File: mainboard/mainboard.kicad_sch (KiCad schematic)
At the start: 52 parts, among them J1 Servo, J2 Buzzer, J4 Button Interface, J5 Power, J6 Release Button, J7 Extra Pins, Q1 BSS138, SW1 SW_Push, U1 RP2040, U2 W25Q128JVS, U3 RV-3028-C7, U4 ITR9608-F, Y1 Crystal_ABM8

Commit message: updated battery footprint
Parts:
- BT1: footprint Battery:BatteryHolder_MPD_BC2003_1x2032 -> Battery:BatteryHolder_Keystone_1060_1x2032
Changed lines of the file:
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@@
 			)
 		)
-		(property "Footprint" "Battery:BatteryHolder_MPD_BC2003_1x2032"
+		(property "Footprint" "Battery:BatteryHolder_Keystone_1060_1x2032"
 			(at 267.97 147.066 90)
 			(effects

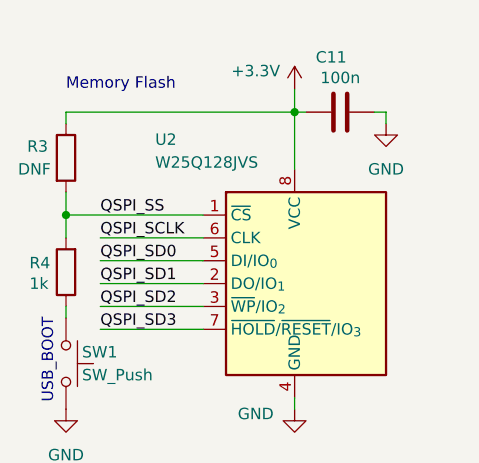
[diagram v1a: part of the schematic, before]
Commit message: switched resistors and capacitors to 0402 and updated pcb
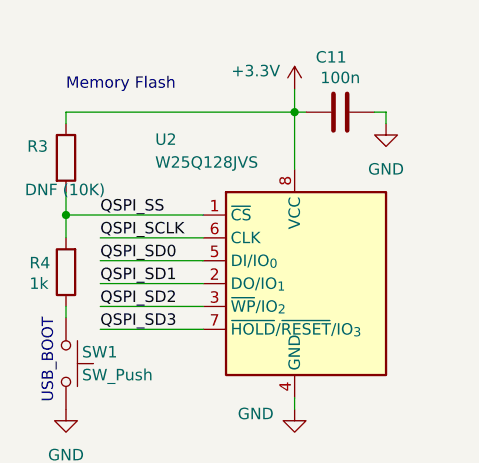
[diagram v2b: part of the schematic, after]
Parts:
- D1, D2: footprint LED_SMD:LED_1206_3216Metric -> LED_SMD:LED_0402_1005Metric
- R10, R11, R12, R13, R22, R6, R7, R8, R9: footprint Resistor_SMD:R_0805_2012Metric -> Resistor_SMD:R_0402_1005Metric
- R14, R4: footprint Resistor_SMD:R_0603_1608Metric -> Resistor_SMD:R_0402_1005Metric
- R3: value DNF -> DNF (10K)
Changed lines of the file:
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@@
 			)
 		)
-		(property "Footprint" "Resistor_SMD:R_0805_2012Metric"
+		(property "Footprint" "Resistor_SMD:R_0402_1005Metric"
 			(at 224.282 100.33 90)
 			(effects
@@
 			)
 		)
-		(property "Footprint" "LED_SMD:LED_1206_3216Metric"
+		(property "Footprint" "LED_SMD:LED_0402_1005Metric"
 			(at 232.41 35.56 0)
 			(effects
@@
 			)
 		)
-		(property "Footprint" "Resistor_SMD:R_0805_2012Metric"
+		(property "Footprint" "Resistor_SMD:R_0402_1005Metric"
 			(at 220.472 135.89 90)
 			(effects
@@
 			)
 		)
-		(property "Footprint" "Resistor_SMD:R_0603_1608Metric"
+		(property "Footprint" "Resistor_SMD:R_0402_1005Metric"
 			(at 23.368 41.91 90)
 			(effects
@@
 			)
 		)
-		(property "Footprint" "Resistor_SMD:R_0805_2012Metric"
+		(property "Footprint" "Resistor_SMD:R_0402_1005Metric"
 			(at 257.302 134.62 90)
 			(effects
@@
 			)
 		)
-		(property "Footprint" "Resistor_SMD:R_0603_1608Metric"
+		(property "Footprint" "Resistor_SMD:R_0402_1005Metric"
 			(at 195.58 41.148 90)
 			(effects
@@
 			)
 		)
-		(property "Footprint" "LED_SMD:LED_1206_3216Metric"
+		(property "Footprint" "LED_SMD:LED_0402_1005Metric"
 			(at 219.71 35.56 0)
 			(effects
@@
 			)
 		)
-		(property "Footprint" "Resistor_SMD:R_0805_2012Metric"
+		(property "Footprint" "Resistor_SMD:R_0402_1005Metric"
 			(at 243.332 100.33 90)
 			(effects
@@
 			)
 		)
-		(property "Footprint" "Resistor_SMD:R_0805_2012Metric"
+		(property "Footprint" "Resistor_SMD:R_0402_1005Metric"
 			(at 60.452 82.55 90)
 			(effects
@@
 			)
 		)
-		(property "Footprint" "Resistor_SMD:R_0805_2012Metric"
+		(property "Footprint" "Resistor_SMD:R_0402_1005Metric"
 			(at 210.312 135.89 90)
 			(effects
@@
 			)
 		)
-		(property "Footprint" "Resistor_SMD:R_0805_2012Metric"
+		(property "Footprint" "Resistor_SMD:R_0402_1005Metric"
 			(at 230.632 27.94 90)
 			(effects
@@
 			)
 		)
-		(property "Footprint" "Resistor_SMD:R_0805_2012Metric"
+		(property "Footprint" "Resistor_SMD:R_0402_1005Metric"
 			(at 160.782 105.41 90)
 			(effects
@@
 			)
 		)
-		(property "Footprint" "Resistor_SMD:R_0805_2012Metric"
+		(property "Footprint" "Resistor_SMD:R_0402_1005Metric"
 			(at 217.932 27.94 90)
 			(effects
@@
 			)
 		)
-		(property "Value" "DNF"
-			(at 16.256 30.48 0)
+		(property "Value" "DNF (10K)"
+			(at 17.018 32.766 0)
 			(effects
 				(font

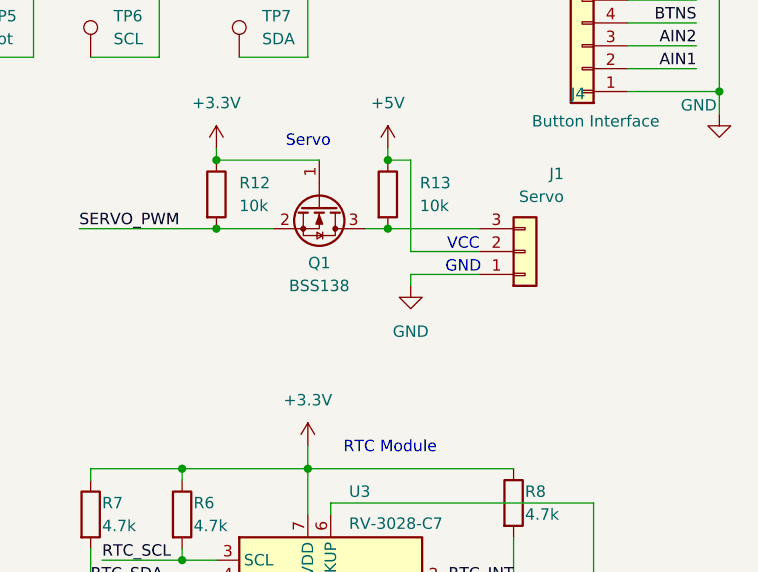
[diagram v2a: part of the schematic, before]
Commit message: added indicator LEDs
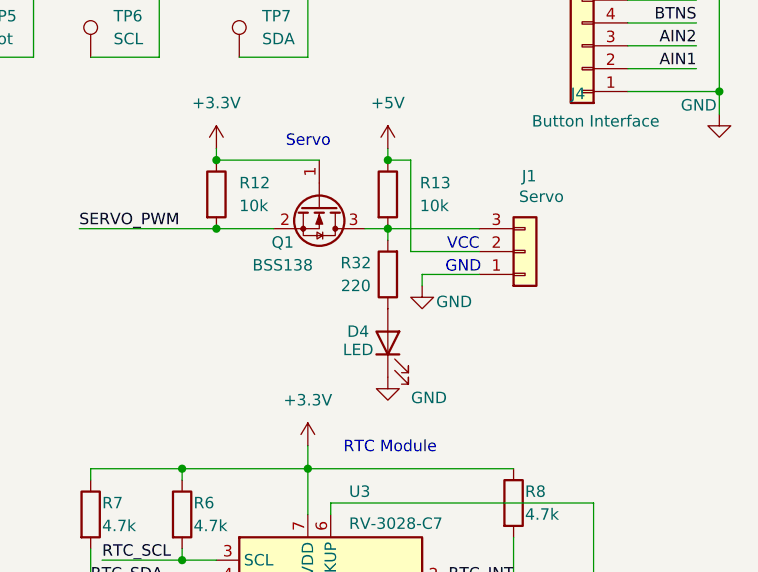
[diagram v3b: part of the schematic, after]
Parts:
- added D4: LED, LED_SMD:LED_0402_1005Metric, symbol Device:LED
- added R32: 220, Resistor_SMD:R_0402_1005Metric, symbol Device:R
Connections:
- net GND: now also D4.1 (K)
- net at J1.3 (Pin_3), Q1.3 (D), R13.2: now also R32.2
- new net: D4.2 (A), R32.1
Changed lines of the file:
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@@
 	(wire
 		(pts
-			(xy 247.65 109.22) (xy 247.65 110.49)
+			(xy 248.92 109.22) (xy 248.92 110.49)
 		)
 		(stroke
@@
 	(wire
 		(pts
-			(xy 247.65 109.22) (xy 255.27 109.22)
+			(xy 248.92 109.22) (xy 255.27 109.22)
 		)
 		(stroke
@@
 	(wire
 		(pts
+			(xy 245.11 104.14) (xy 245.11 105.41)
+		)
+		(stroke
+			(width 0)
+			(type default)
+		)
+	)
+	(wire
+		(pts
 			(xy 71.12 72.39) (xy 71.12 76.2)
 		)
@@
 		(dnp no)
 		(property "Reference" "J1"
-			(at 264.668 98.044 0)
+			(at 261.62 98.298 0)
 			(effects
 				(font
@@
 	)
 	(symbol
+		(lib_id "Device:LED")
+		(at 245.11 116.84 90)
+		(unit 1)
+		(exclude_from_sim no)
+		(in_bom yes)
+		(on_board yes)
+		(dnp no)
+		(property "Reference" "D4"
+			(at 241.808 115.57 90)
+			(effects
+				(font
+					(size 1.27 1.27)
+				)
+			)
+		)
+		(property "Value" "LED"
+			(at 241.808 117.602 90)
+			(effects
+				(font
+					(size 1.27 1.27)
+				)
+			)
+		)
+		(property "Footprint" "LED_SMD:LED_0402_1005Metric"
+			(at 245.11 116.84 0)
+			(effects
+				(font
+					(size 1.27 1.27)
+				)
+				(hide yes)
+			)
+		)
+		(property "Datasheet" "~"
+			(at 245.11 116.84 0)
+			(effects
+				(font
+					(size 1.27 1.27)
+				)
+				(hide yes)
+			)
+		)
+		(property "Description" "White LED"
+			(at 245.11 116.84 0)
+			(effects
+				(font
+					(size 1.27 1.27)
+				)
+				(hide yes)
+			)
+		)
+		(property "Sim.Pins" "1=K 2=A"
+			(at 245.11 116.84 0)
+			(effects
+				(font
+					(size 1.27 1.27)
+				)
+				(hide yes)
+			)
+		)
+		(pin "2"
+		)
+		(pin "1"
+		)
+		(instances
+			(project "mainboard"
+				(path "/57f2b6ac-3611-4b16-b8a1-8e91b00e0208"
+					(reference "D4")
+					(unit 1)
+				)
+			)
+		)
+	)
+	(symbol
 		(lib_id "Device:R")
 		(at 21.59 41.91 180)
@@
 		(on_board yes)
 		(dnp no)
-		(fields_autoplaced yes)
 		(property "Reference" "Q1"
-			(at 237.49 107.95 90)
+			(at 233.426 105.664 90)
 			(effects
 				(font
@@
 		)
 		(property "Value" "BSS138"
-			(at 237.49 110.49 90)
+			(at 233.426 108.204 90)
 			(effects
 				(font
@@
 	)
 	(symbol
+		(lib_id "power:GND")
+		(at 245.11 120.65 0)
+		(unit 1)
+		(exclude_from_sim no)
+		(in_bom yes)
+		(on_board yes)
+		(dnp no)
+		(property "Reference" "#PWR035"
+			(at 245.11 127 0)
+			(effects
+				(font
+					(size 1.27 1.27)
+				)
+				(hide yes)
+			)
+		)
+		(property "Value" "GND"
+			(at 249.682 122.936 0)
+			(effects
+				(font
+					(size 1.27 1.27)
+				)
+			)
+		)
+		(property "Footprint" ""
+			(at 245.11 120.65 0)
+			(effects
+				(font
+					(size 1.27 1.27)
+				)
+				(hide yes)
+			)
+		)
+		(property "Datasheet" ""
+			(at 245.11 120.65 0)
+			(effects
+				(font
+					(size 1.27 1.27)
+				)
+				(hide yes)
+			)
+		)
+		(property "Description" "Power symbol creates a global label with name \"GND\" , ground"
+			(at 245.11 120.65 0)
+			(effects
+				(font
+					(size 1.27 1.27)
+				)
+				(hide yes)
+			)
+		)
+		(pin "1"
+		)
+		(instances
+			(project ""
+				(path "/57f2b6ac-3611-4b16-b8a1-8e91b00e0208"
+					(reference "#PWR035")
+					(unit 1)
+				)
+			)
+		)
+	)
+	(symbol
 		(lib_id "Device:C")
 		(at 109.22 53.34 180)
@@
 	(symbol
 		(lib_id "power:GND")
-		(at 247.65 110.49 0)
+		(at 248.92 110.49 0)
 		(unit 1)
 		(exclude_from_sim no)
@@
 		(on_board yes)
 		(dnp no)
-		(fields_autoplaced yes)
 		(property "Reference" "#PWR013"
-			(at 247.65 116.84 0)
+			(at 248.92 116.84 0)
 			(effects
 				(font
@@
 		)
 		(property "Value" "GND"
-			(at 247.65 115.57 0)
+			(at 252.476 112.268 0)
 			(effects
 				(font
@@
 		)
 		(property "Footprint" ""
-			(at 247.65 110.49 0)
+			(at 248.92 110.49 0)
 			(effects
 				(font
@@
 		)
 		(property "Datasheet" ""
-			(at 247.65 110.49 0)
+			(at 248.92 110.49 0)
 			(effects
 				(font
@@
 		)
 		(property "Description" "Power symbol creates a global label with name \"GND\" , ground"
-			(at 247.65 110.49 0)
+			(at 248.92 110.49 0)
 			(effects
 				(font
@@
 					(unit 1)
 				)
+			)
+		)
+	)
+	(symbol
+		(lib_id "Device:R")
+		(at 245.11 109.22 180)
+		(unit 1)
+		(exclude_from_sim no)
+		(in_bom yes)
+		(on_board yes)
+		(dnp no)
+		(property "Reference" "R32"
+			(at 241.554 107.95 0)
+			(effects
+				(font
+					(size 1.27 1.27)
+				)
+			)
+		)
+		(property "Value" "220"
+			(at 241.554 110.49 0)
+			(effects
+				(font
+					(size 1.27 1.27)
+				)
+			)
+		)
+		(property "Footprint" "Resistor_SMD:R_0402_1005Metric"
+			(at 246.888 109.22 90)
+			(effects
+				(font
+					(size 1.27 1.27)
+				)
+				(hide yes)
+			)
+		)
+		(property "Datasheet" "~"
+			(at 245.11 109.22 0)
+			(effects
+				(font
+					(size 1.27 1.27)
+				)
+				(hide yes)
+			)
+		)
+		(property "Description" "Resistor"
+			(at 245.11 109.22 0)
+			(effects
+				(font
+					(size 1.27 1.27)
+				)
+				(hide yes)
+			)
+		)
+		(pin "2"
+		)
+		(pin "1"
+		)
+		(instances
+			(project "mainboard"
+				(path "/57f2b6ac-3611-4b16-b8a1-8e91b00e0208"
+					(reference "R32")
+					(unit 1)
+				)

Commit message: Minor fixes
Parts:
- removed R12: 10k, Resistor_SMD:R_0402_1005Metric, symbol Device:R
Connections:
- net +3.3V: no longer Q1.1 (G)
- net GND: now also Q1.2 (S)
- net SERVO_PWM: now also Q1.1 (G), R32.2; no longer Q1.2 (S)
- net at J1.3 (Pin_3), Q1.3 (D): no longer R13.2, R32.2
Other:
- moved on the sheet: D4, J1, Q1, R13, R32
